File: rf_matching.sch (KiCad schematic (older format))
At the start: 12 parts, among them J1 RFI, J2 RFO, J3 CTRL, J4 ANT, J5 3V3, U1 pe4259ds, U2 SF2098

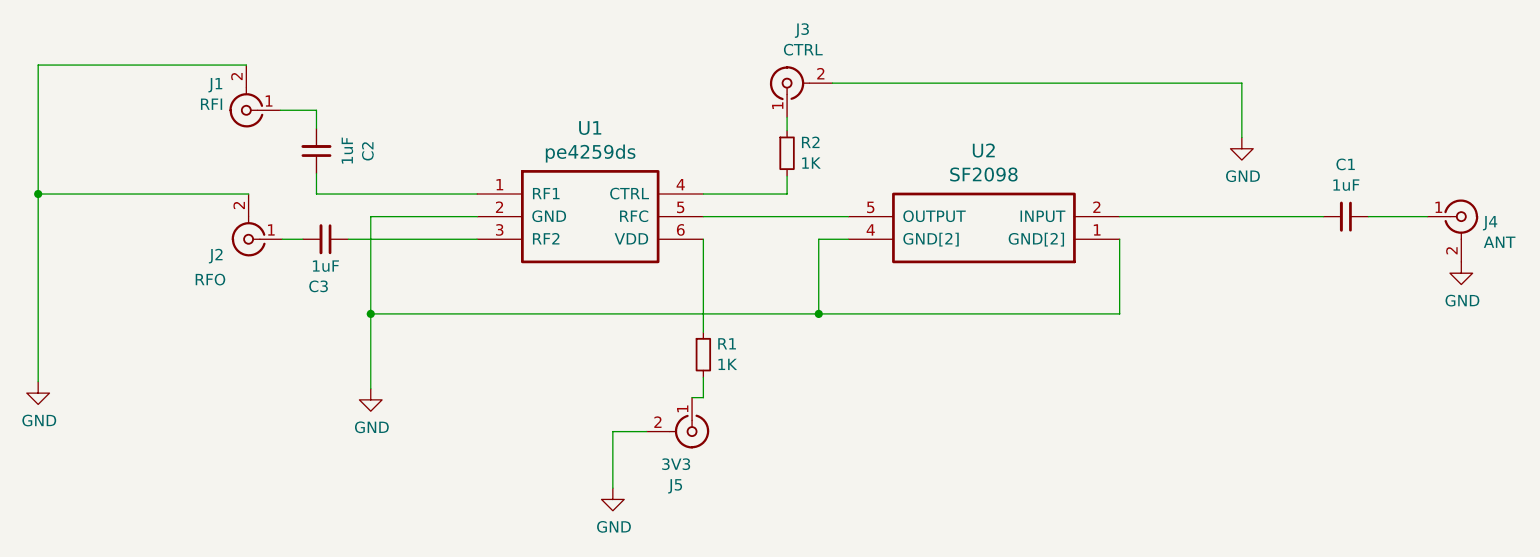
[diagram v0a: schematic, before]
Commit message: Version with the board with just the saw filter, no vias yet
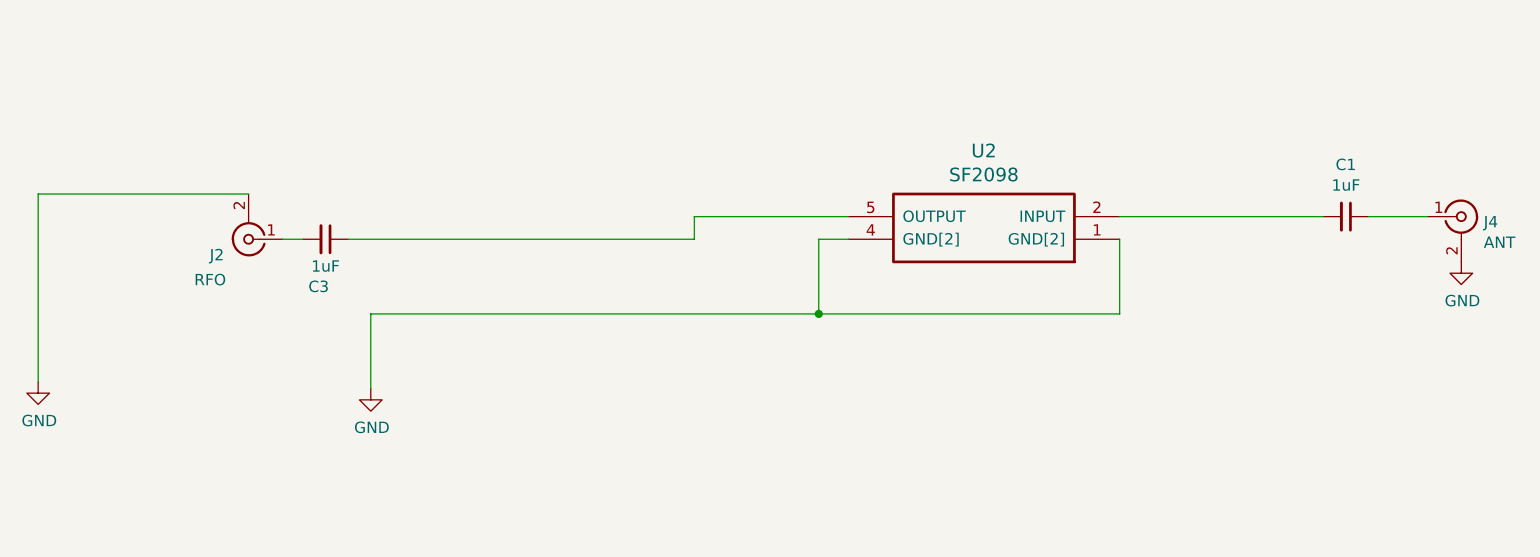
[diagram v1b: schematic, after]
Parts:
- removed C2: 1uF, KiCad/Capacitors_SMD.pretty:C_0603, symbol C_Small
- removed J1: RFI, KiCad/Connectors_Molex.pretty:Molex_SMA_Jack_Edge_Mount, symbol Conn_Coaxial
- removed J3: CTRL, KiCad/Connectors_Molex.pretty:Molex_SMA_Jack_Edge_Mount, symbol Conn_Coaxial
- removed J5: 3V3, KiCad/Connectors_Molex.pretty:Molex_SMA_Jack_Edge_Mount, symbol Conn_Coaxial
- removed R1, R2: 1K, KiCad/Resistors_SMD.pretty:R_0603, symbol R_Small
- removed U1: pe4259ds, OLIMEX/KiCAD/KiCAD_Footprints/OLIMEX_IC-FP.pretty:SC70-6_Pitch-0.65_2.00x2.10x1.00mm, symbol pe4259ds
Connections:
- net at U2.5 (OUTPUT): now also C3.1
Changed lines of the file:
@@
-$EndComp
-$Comp
-L Conn_Coaxial J1
-U 1 1 5B4ACFC6
-P 3010 3680
-F 0 "J1" H 3110 3564 50  0000 L CNN
-F 1 "RFI" H 3110 3655 50  0000 L CNN
-F 2 "KiCad/Connectors_Molex.pretty:Molex_SMA_Jack_Edge_Mount" H 3010 3680 50  0001 C CNN
-F 3 "" H 3010 3680 50  0001 C CNN
-	1    3010 3680
-	-1   0    0    1
 $EndComp
 $Comp
@@
 $EndComp
 $Comp
-L Conn_Coaxial J3
-U 1 1 5B4AD06B
-P 5400 3560
-F 0 "J3" V 5637 3490 50  0000 C CNN
-F 1 "CTRL" V 5546 3490 50  0000 C CNN
-F 2 "KiCad/Connectors_Molex.pretty:Molex_SMA_Jack_Edge_Mount" H 5400 3560 50  0001 C CNN
-F 3 "" H 5400 3560 50  0001 C CNN
-	1    5400 3560
-	0    -1   -1   0
-$EndComp
-$Comp
 L Conn_Coaxial J4
 U 1 1 5B4AD0BF
@@
 F 3 "" H 8380 4150 50  0001 C CNN
 	1    8380 4150
-	1    0    0    -1
-$EndComp
-$Comp
-L pe4259ds U1
-U 1 1 5B4AD2A2
-P 4030 4050
-F 0 "U1" H 4530 4340 60  0000 C CNN
-F 1 "pe4259ds" H 4530 4234 60  0000 C CNN
-F 2 "OLIMEX/KiCAD/KiCAD_Footprints/OLIMEX_IC-FP.pretty:SC70-6_Pitch-0.65_2.00x2.10x1.00mm" H 4030 4050 60  0001 C CNN
-F 3 "" H 4030 4050 60  0001 C CNN
-	1    4030 4050
 	1    0    0    -1
 $EndComp
@@
 	1    0    0    -1
 $EndComp
-$Comp
-L GND #PWR04
-U 1 1 5B4AE57C
-P 7410 3800
-F 0 "#PWR04" H 7410 3550 50  0001 C CNN
-F 1 "GND" H 7415 3627 50  0000 C CNN
-F 2 "" H 7410 3800 50  0001 C CNN
-F 3 "" H 7410 3800 50  0001 C CNN
-	1    7410 3800
-	1    0    0    -1
-$EndComp
-$Comp
-L Conn_Coaxial J5
-U 1 1 5B4AF99C
-P 4980 5100
-F 0 "J5" V 5217 5030 50  0000 C CNN
-F 1 "3V3" V 5126 5030 50  0000 C CNN
-F 2 "KiCad/Connectors_Molex.pretty:Molex_SMA_Jack_Edge_Mount" H 4980 5100 50  0001 C CNN
-F 3 "" H 4980 5100 50  0001 C CNN
-	1    4980 5100
-	0    1    1    0
-$EndComp
-$Comp
-L GND #PWR03
-U 1 1 5B4AFA81
-P 4630 5350
-F 0 "#PWR03" H 4630 5100 50  0001 C CNN
-F 1 "GND" H 4635 5177 50  0000 C CNN
-F 2 "" H 4630 5350 50  0001 C CNN
-F 3 "" H 4630 5350 50  0001 C CNN
-	1    4630 5350
-	1    0    0    -1
-$EndComp
-$Comp
-L R_Small R2
-U 1 1 5B4B4209
-P 5400 3870
-F 0 "R2" H 5459 3916 50  0000 L CNN
-F 1 "1K" H 5459 3825 50  0000 L CNN
-F 2 "KiCad/Resistors_SMD.pretty:R_0603" H 5400 3870 50  0001 C CNN
-F 3 "" H 5400 3870 50  0001 C CNN
-	1    5400 3870
-	1    0    0    -1
-$EndComp
-$Comp
-L R_Small R1
-U 1 1 5B4B42FE
-P 5030 4760
-F 0 "R1" H 5089 4806 50  0000 L CNN
-F 1 "1K" H 5089 4715 50  0000 L CNN
-F 2 "KiCad/Resistors_SMD.pretty:R_0603" H 5030 4760 50  0001 C CNN
-F 3 "" H 5030 4760 50  0001 C CNN
-	1    5030 4760
-	1    0    0    -1
-$EndComp
 Wire Wire Line
-	5670 4150 5030 4150
-Wire Wire Line
-	4030 4150 3560 4150
-Wire Wire Line
-	3560 4150 3560 4910
-Wire Wire Line
-	4030 4050 3320 4050
-Wire Wire Line
-	3320 3680 3160 3680
+	4990 4150 5670 4150
 Wire Wire Line
 	3020 4050 2090 4050
-Wire Wire Line
-	2090 3480 2090 4880
-Wire Wire Line
-	3010 3480 2090 3480
-Connection ~ 2090 4050
 Wire Wire Line
 	6870 4580 6870 4250
 Wire Wire Line
 	3560 4580 6870 4580
-Connection ~ 3560 4580
 Wire Wire Line
 	5670 4250 5540 4250
@@
 	5540 4250 5540 4580
 Connection ~ 5540 4580
-Wire Wire Line
-	5030 4050 5400 4050
-Wire Wire Line
-	5600 3560 7410 3560
-Wire Wire Line
-	7410 3560 7410 3800
-Wire Wire Line
-	4780 5100 4630 5100
-Wire Wire Line
-	4630 5100 4630 5350
-Wire Wire Line
-	5030 4950 4980 4950
-Wire Wire Line
-	5400 4050 5400 3970
-Wire Wire Line
-	5400 3710 5400 3770
-Wire Wire Line
-	5030 4950 5030 4860
-Wire Wire Line
-	5030 4660 5030 4250
 $Comp
 L C_Small C1
@@
 	7770 4150 6870 4150
 $Comp
-L C_Small C2
-U 1 1 5B5135C2
-P 3320 3860
-F 0 "C2" V 3091 3860 50  0000 C CNN
-F 1 "1uF" V 3182 3860 50  0000 C CNN
-F 2 "KiCad/Capacitors_SMD.pretty:C_0603" H 3320 3860 50  0001 C CNN
-F 3 "" H 3320 3860 50  0001 C CNN
-	1    3320 3860
-	-1   0    0    1
-$EndComp
-$Comp
 L C_Small C3
 U 1 1 5B5136C2
@@
 $EndComp
 Wire Wire Line
-	4030 4250 3460 4250
+	3460 4250 4990 4250
 Wire Wire Line
 	3260 4250 3170 4250
 Wire Wire Line
-	3320 4050 3320 3960
+	2090 4050 2090 4880
 Wire Wire Line
-	3320 3680 3320 3760
+	4990 4250 4990 4150
+Wire Wire Line
+	3560 4580 3560 4910
 $EndSCHEMATC
